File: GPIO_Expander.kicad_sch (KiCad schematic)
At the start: 2 parts, among them U3 TCA9535PWR

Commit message: added routing and gerber
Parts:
- added J10, J11, J12, J13, J14, J15, J16, J4, J5, J6, J7, J8, J9: Conn_01x03_Pin, Connector_JST:JST_XH_S3B-XH-A_1x03_P2.50mm_Horizontal, symbol Connector:Conn_01x03_Pin
- renumbered C3 to C6, U3 to U4
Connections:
- net +3V3: now also J10.3 (Pin_3), J11.3 (Pin_3), J12.3 (Pin_3), J13.3 (Pin_3), J14.3 (Pin_3), J15.3 (Pin_3), J16.3 (Pin_3), J4.3 (Pin_3), J5.3 (Pin_3), J6.3 (Pin_3), J7.3 (Pin_3), J8.3 (Pin_3), J9.3 (Pin_3)
- net GND: now also J10.1 (Pin_1), J11.1 (Pin_1), J12.1 (Pin_1), J13.1 (Pin_1), J14.1 (Pin_1), J15.1 (Pin_1), J16.1 (Pin_1), J4.1 (Pin_1), J5.1 (Pin_1), J6.1 (Pin_1), J7.1 (Pin_1), J8.1 (Pin_1), J9.1 (Pin_1)
- net P00: now also J4.2 (Pin_2)
- net P01: now also J5.2 (Pin_2)
- net P02: now also J6.2 (Pin_2)
- net P03: now also J7.2 (Pin_2)
- net P04: now also J8.2 (Pin_2)
- net P05: now also J9.2 (Pin_2)
- net P06: now also J10.2 (Pin_2)
- net P07: now also J11.2 (Pin_2)
- net P10: now also J12.2 (Pin_2)
- net P11: now also J13.2 (Pin_2)
- net P12: now also J14.2 (Pin_2)
- net P13: now also J15.2 (Pin_2)
- net P14: now also J16.2 (Pin_2)
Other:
- removed sheet In Out Stage #1
- note added: "Connectors"

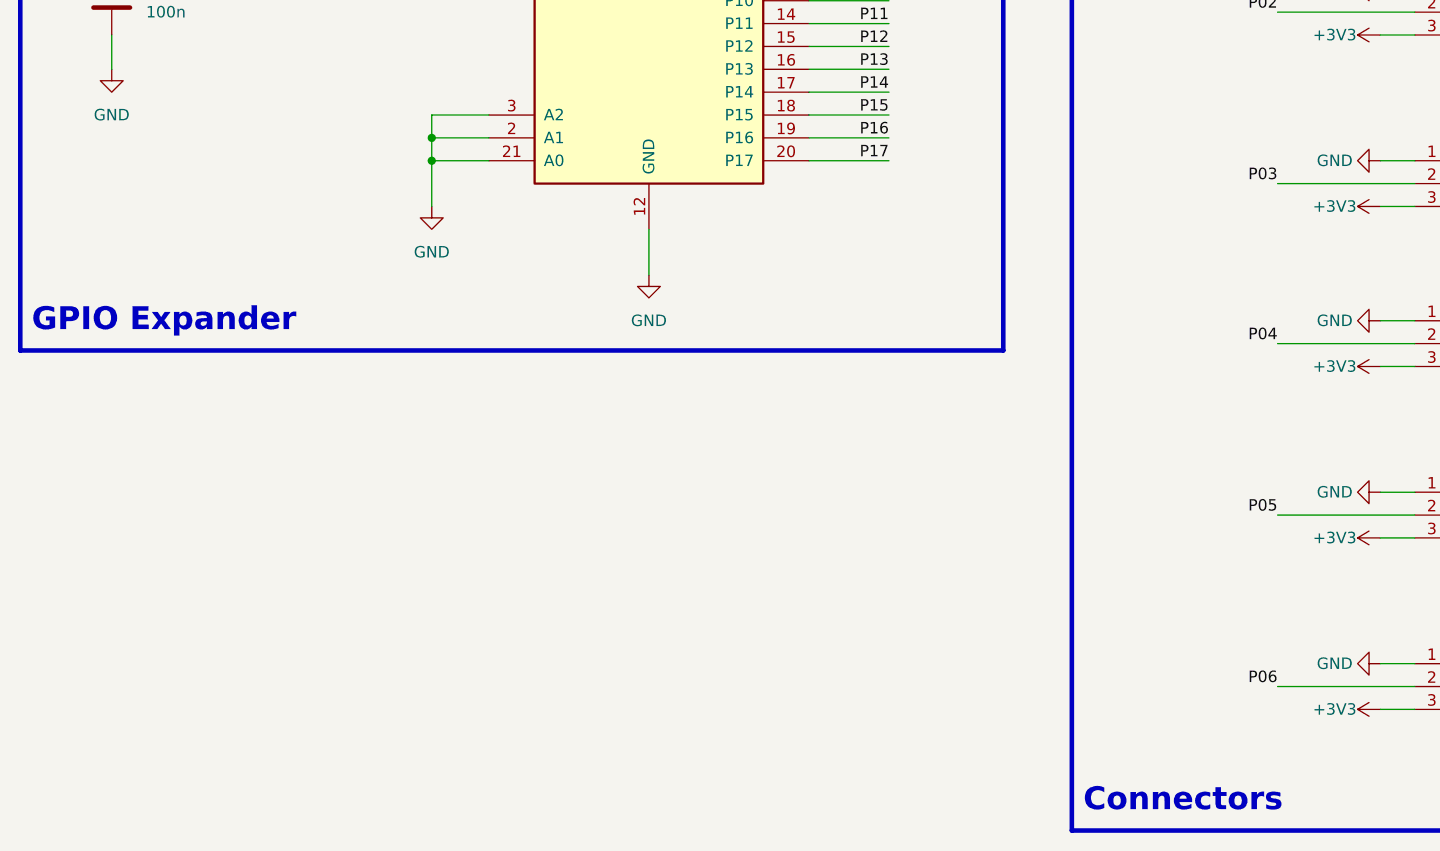
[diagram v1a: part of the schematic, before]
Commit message: added adc
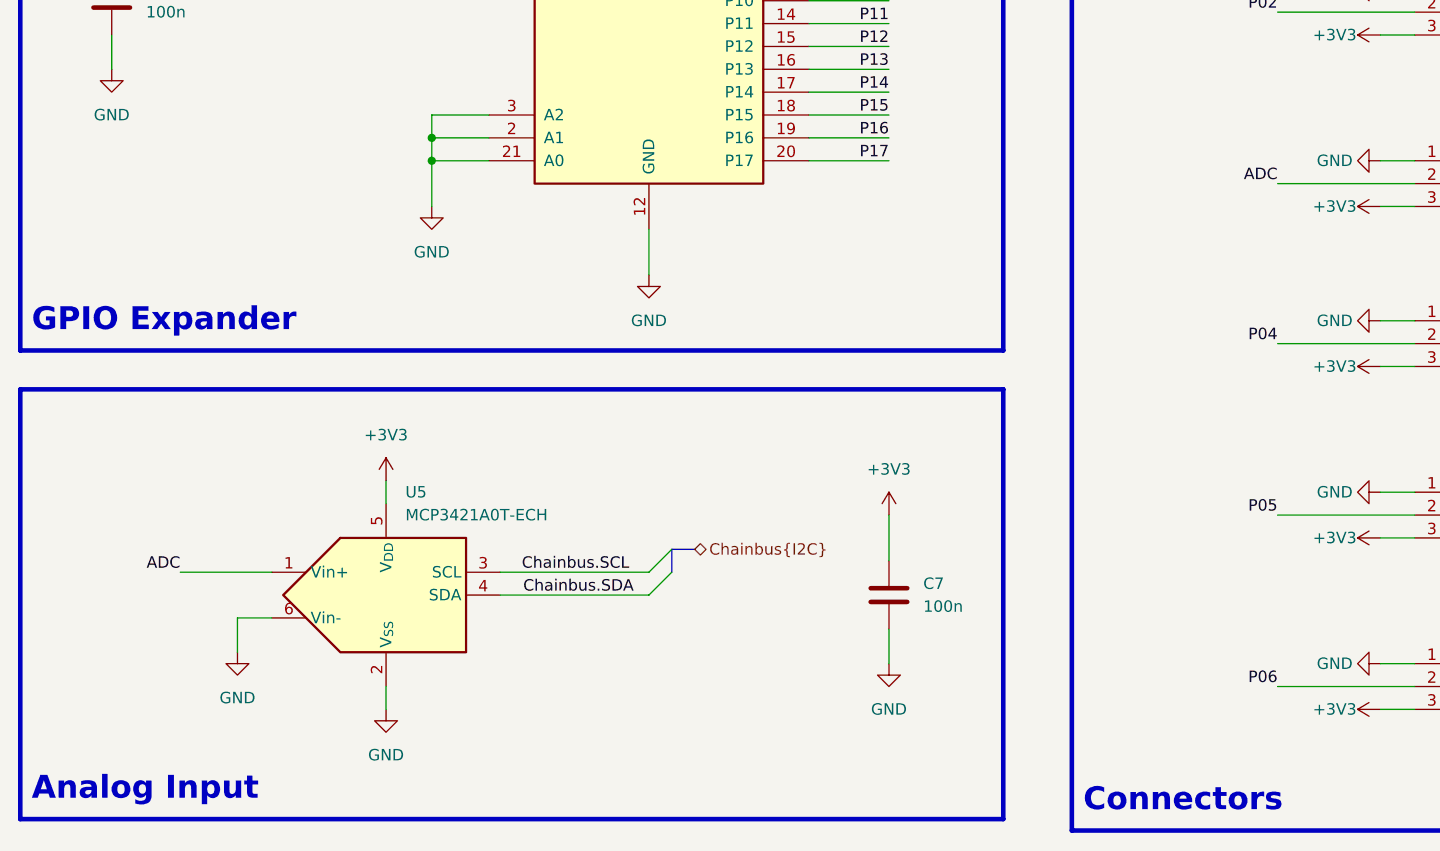
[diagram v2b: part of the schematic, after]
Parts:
- added C7: 100n, PCM_JLCPCB:C_0603, symbol Device:C
- added U5: MCP3421A0T-ECH, Package_TO_SOT_SMD:SOT-23-6, symbol Analog_ADC:MCP3421A0T-ECH
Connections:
- net +3V3: now also C7.1, U5.5 (V_{DD})
- net Chainbus.SCL: now also U5.3 (SCL)
- net Chainbus.SDA: now also U5.4 (SDA)
- net GND: now also C7.2, U5.2 (V_{SS}), U5.6 (Vin-)
- net P03: no longer J7.2 (Pin_2)
- new net ADC: J7.2 (Pin_2), U5.1 (Vin+)
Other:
- note added: "Analog Input"

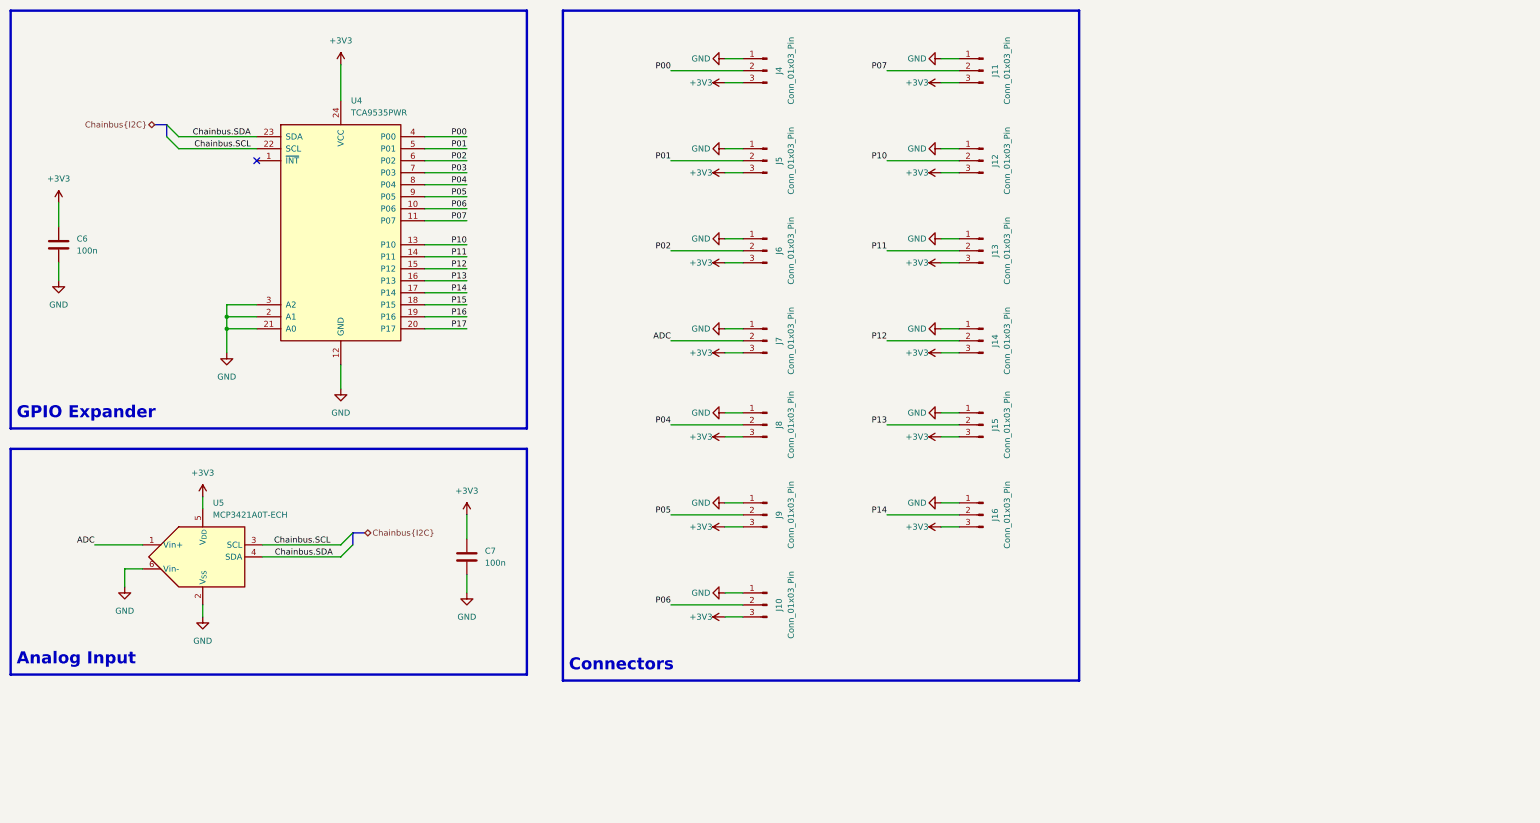
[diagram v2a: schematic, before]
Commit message: added leds and bom. Revison 1.2
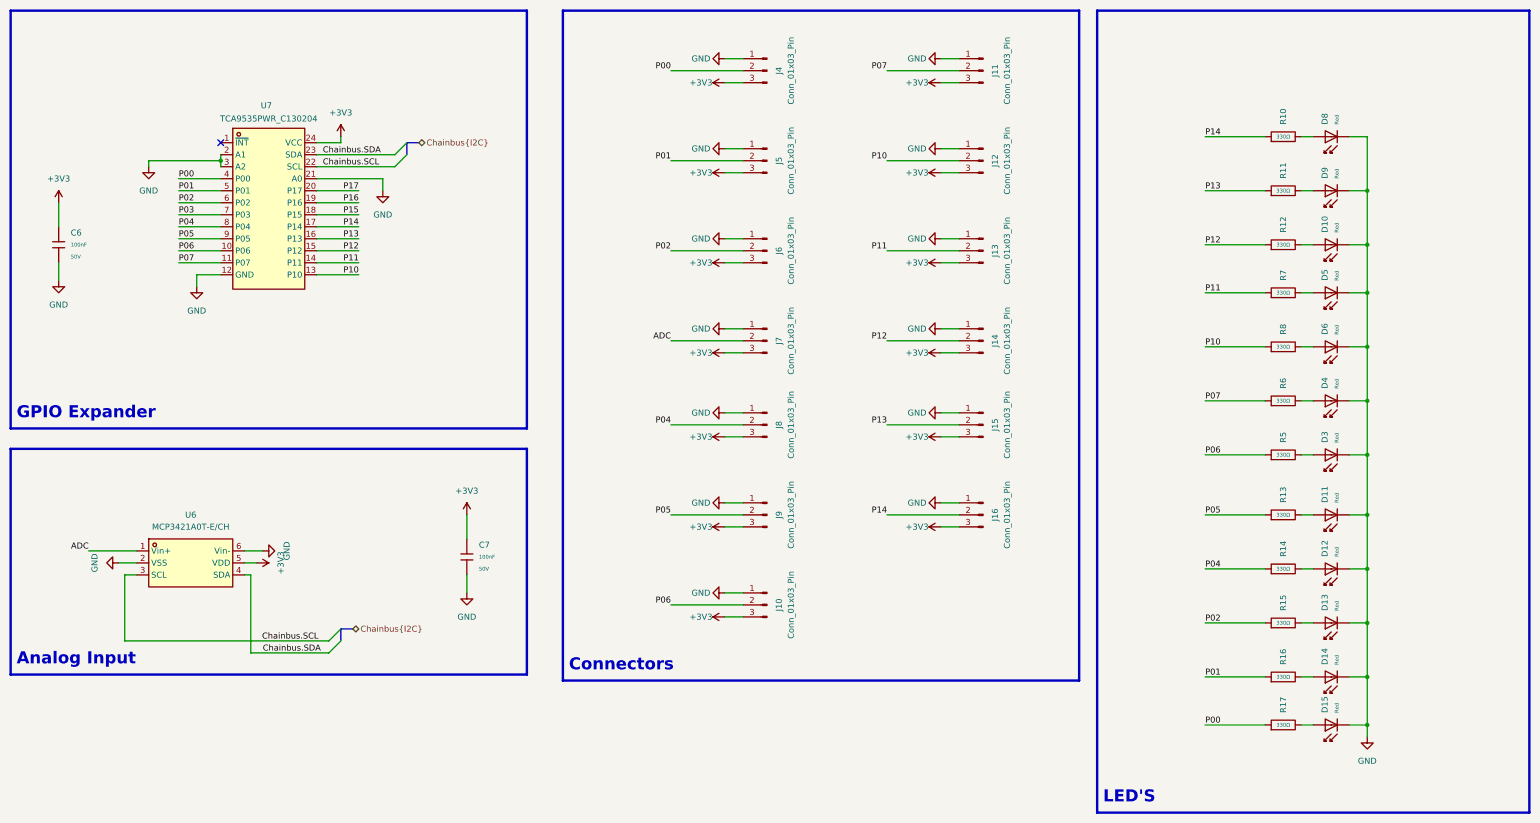
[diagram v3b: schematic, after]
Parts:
- removed C6, C7: 100n, PCM_JLCPCB:C_0603, symbol Device:C
- removed U4: TCA9535PWR, Package_SO:TSSOP-24_4.4x7.8mm_P0.65mm, symbol Interface_Expansion:TCA9535PWR
- removed U5: MCP3421A0T-ECH, Package_TO_SOT_SMD:SOT-23-6, symbol Analog_ADC:MCP3421A0T-ECH
- added C6, C7: 100nF, PCM_JLCPCB:C_0603, symbol PCM_JLCPCB-Capacitors:0603,100nF
- added D10, D11, D12, D13, D14, D15, D3, D4, D5, D6, D8, D9: Red, PCM_JLCPCB:D_0603, symbol PCM_JLCPCB-Diodes:LED,0603,Red
- added R10, R11, R12, R13, R14, R15, R16, R17, R5, R6, R7, R8: 330Ω, PCM_JLCPCB:R_0402, symbol PCM_JLCPCB-Resistors:0402,330Ω
- added U6: MCP3421A0T-E/CH, MCP3421A0T:SOT-23-6_L2.9-W1.6-P0.95-LS2.8-BR, symbol MCP3421A0T:MCP3421A0T-E_CH
- added U7: TCA9535PWR_C130204, TCA9535PWR:TSSOP-24_L7.8-W4.4-P0.65-LS6.4-BL, symbol TCA9535PWR1_new_footprint:TCA9535PWR_C130204
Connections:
- net +3V3: now also C6.1, C7.1, U6.5 (VDD), U7.24 (VCC)
- net ADC: now also U6.1 (Vin+)
- net Chainbus.SCL: now also U6.3 (SCL), U7.22 (SCL)
- net Chainbus.SDA: now also U6.4 (SDA), U7.23 (SDA)
- net GND: now also C6.2, C7.2, D10.1, D11.1, D12.1, D13.1, D14.1, D15.1, D3.1, D4.1, D5.1, D6.1, D8.1, D9.1, U6.2 (VSS), U6.6 (Vin-), U7.12 (GND), U7.2 (A1), U7.21 (A0), U7.3 (A2)
- net P00: now also R17.1, U7.4 (P00)
- net P01: now also R16.1, U7.5 (P01)
- net P02: now also R15.1, U7.6 (P02)
- net P03: now also U7.7 (P03)
- net P04: now also R14.1, U7.8 (P04)
- net P05: now also R13.1, U7.9 (P05)
- net P06: now also R5.1, U7.10 (P06)
- net P07: now also R6.1, U7.11 (P07)
- net P10: now also R8.1, U7.13 (P10)
- net P11: now also R7.1, U7.14 (P11)
- net P12: now also R12.1, U7.15 (P12)
- net P13: now also R11.1, U7.16 (P13)
- net P14: now also R10.1, U7.17 (P14)
- net P15: now also U7.18 (P15)
- net P16: now also U7.19 (P16)
- net P17: now also U7.20 (P17)
- new net: D12.2, R14.2
- new net: D10.2, R12.2
- new net: D3.2, R5.2
- new net: D4.2, R6.2
- new net: D13.2, R15.2
- new net: D11.2, R13.2
- new net: D15.2, R17.2
- new net: D8.2, R10.2
- new net: D5.2, R7.2
- new net: D6.2, R8.2
- new net: D14.2, R16.2
- new net: D9.2, R11.2
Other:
- note added: "LED'S"
